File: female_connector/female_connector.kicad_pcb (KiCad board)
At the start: 2 copper layers, 40.6 x 22.2 mm, 6 parts, among them J1 Conn_02x07_Row_Letter_Last, J2 Conn_02x12_Row_Letter_Last

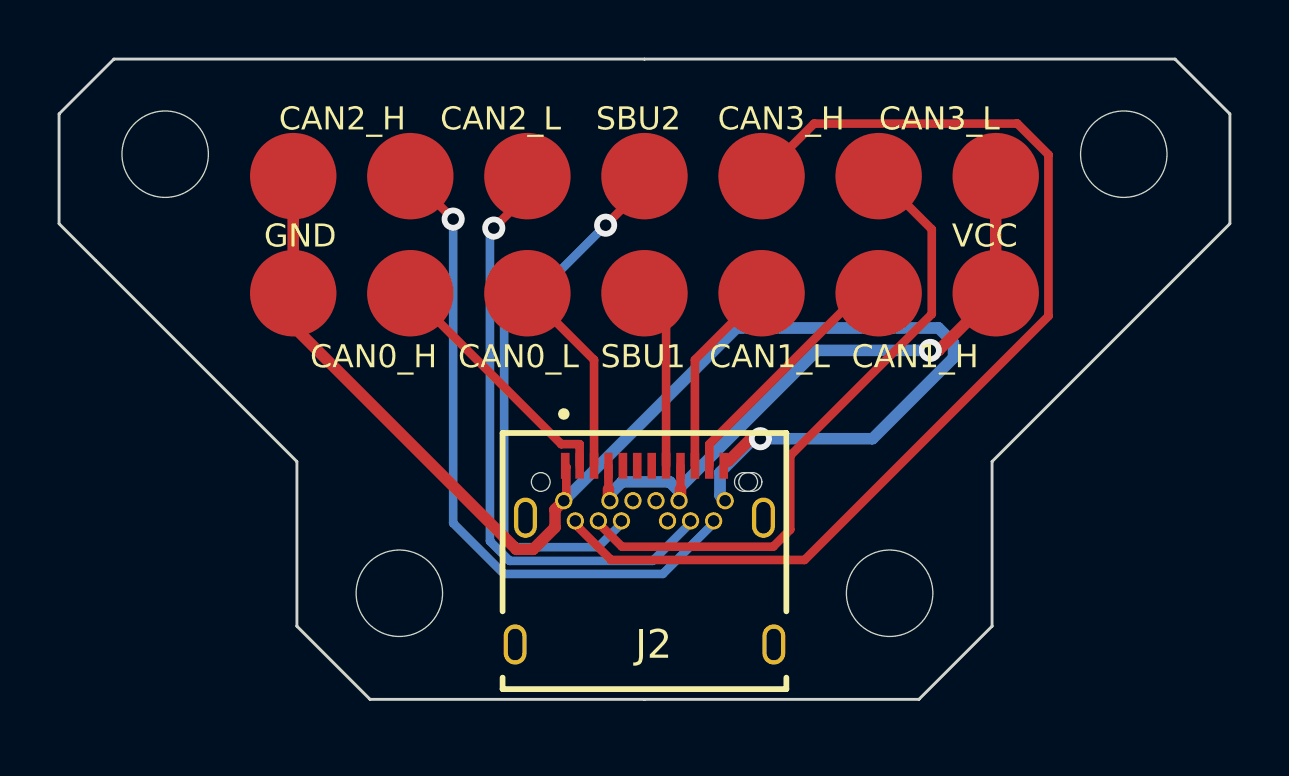
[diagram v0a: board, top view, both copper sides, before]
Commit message: change usb c connector export to jlcpcb
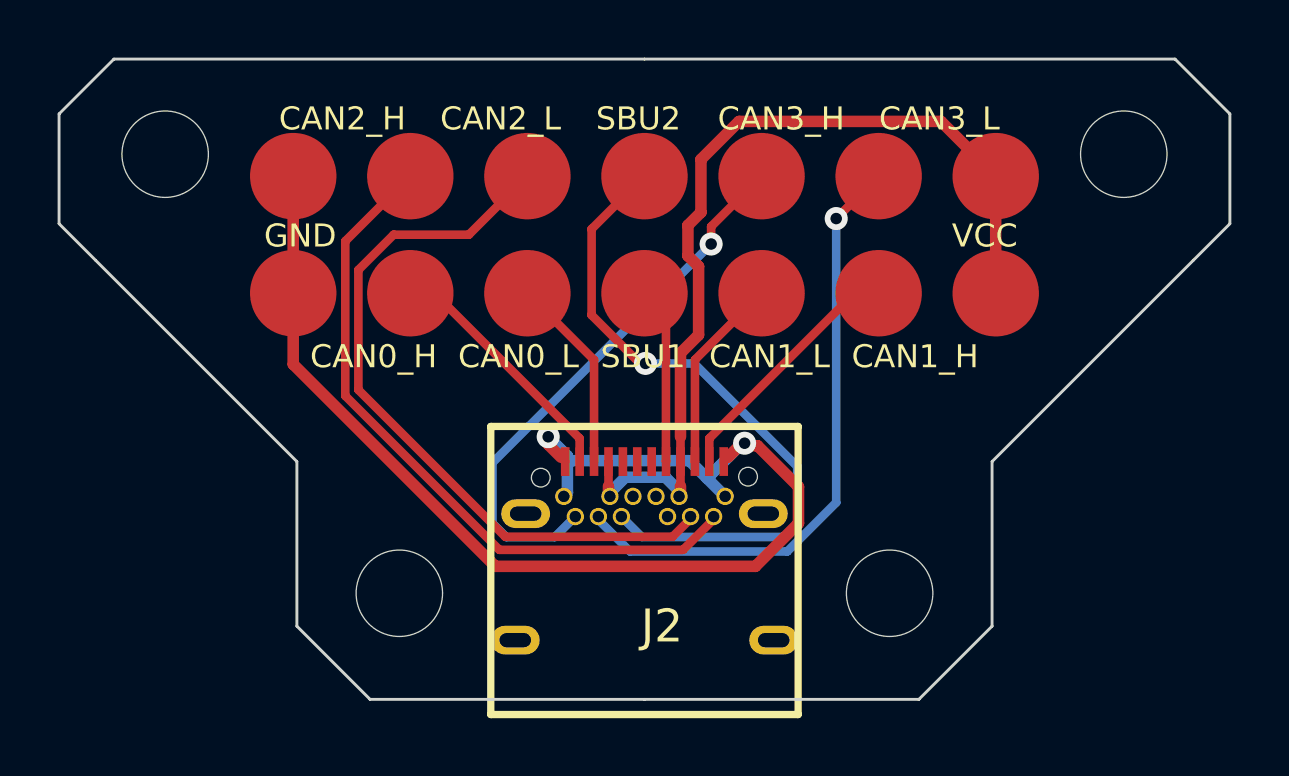
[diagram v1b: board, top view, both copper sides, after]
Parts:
- J2: footprint CommaPogo_Library:GCT_USB4056-03-A_REVA2 -> CommaPogo_Library:USB-C-SMD_HC005-1A1H1A103-0HR
- moved J2 3.25 mm to (140.3, 90.7)
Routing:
- net /CAN3_H: track 37.3 -> 19.3 mm, vias 0 -> 1
- net +12V: track 23.7 -> 32.3 mm, vias 1 -> 0
- net GND: track 49.3 -> 43.7 mm, vias 1 -> 2
- net /SBU2: track 19.2 -> 23.5 mm
- net /CAN2_L: track 21.1 -> 25.4 mm, vias 1 -> 0
- net /CAN3_L: track 22.4 -> 21.5 mm, vias 0 -> 1
- net /CAN2_H: track 23.2 -> 24.1 mm, vias 1 -> 0
